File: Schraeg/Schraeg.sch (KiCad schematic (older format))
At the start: 56 parts, among them U1 TL074, U2 TL074, U3 V2164

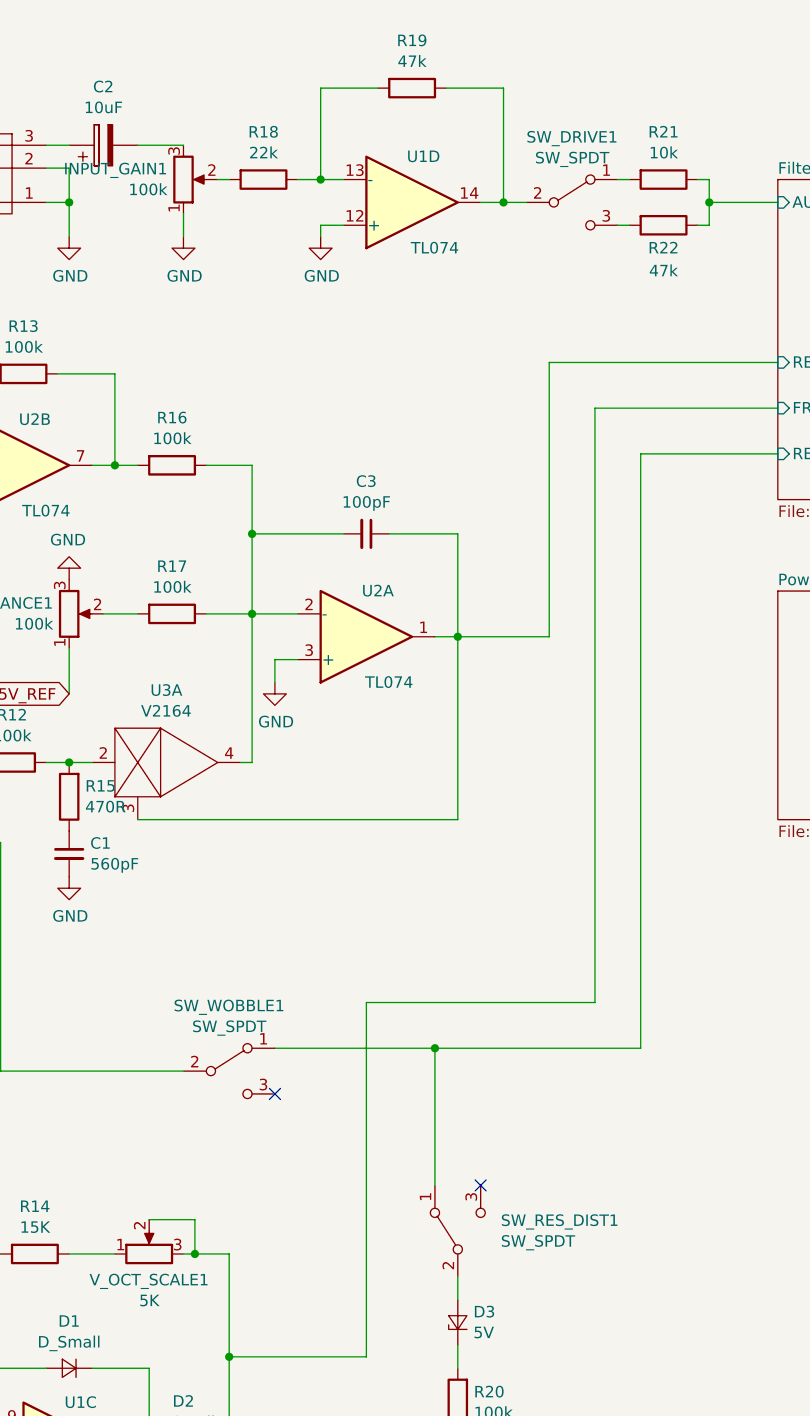
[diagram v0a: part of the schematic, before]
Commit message: Finished v0.2
* Flipped switches
* Enlarged switch holes
* Enlarged and enovaled pot support holes
* Reduced jack socket hole sizes
* Improved component and component reference locations

Archived v0.1 (previously know as the 2019 edition) and
re-exported schematics, gerbers, interactive BOM etc for
the 2021 Edition (v0.2).
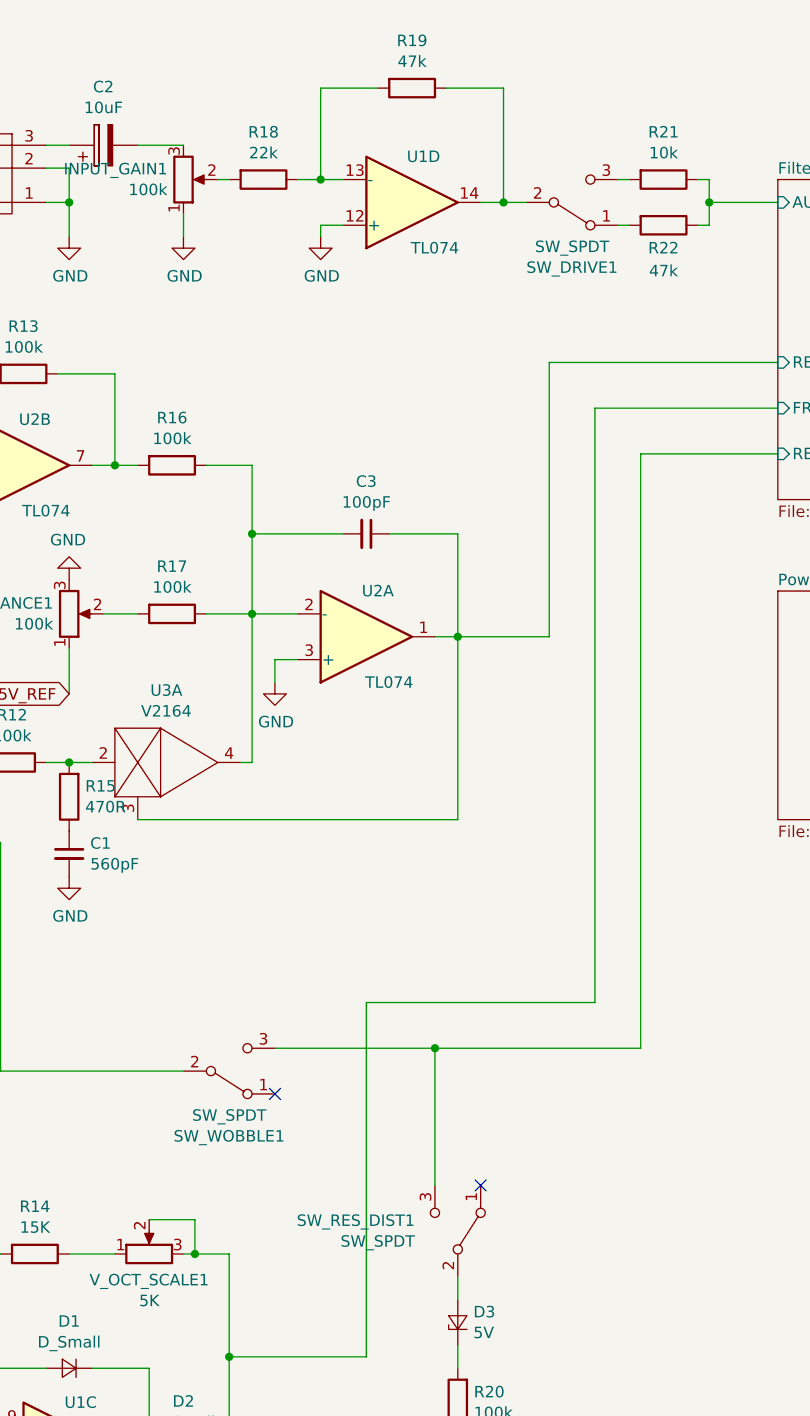
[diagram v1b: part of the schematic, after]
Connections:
- net Filter Core/RES_MOD: now also SW_RES_DIST1.3 (C), SW_WOBBLE1.3 (C); no longer SW_RES_DIST1.1 (A), SW_WOBBLE1.1 (A)
- net at SW_DRIVE1.1 (A): now also R22.2; no longer R21.2
- net at SW_DRIVE1.3 (C): now also R21.2; no longer R22.2
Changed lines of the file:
@@
 F 3 "" H 6500 1500 50  0001 C CNN
 	1    6500 1500
-	1    0    0    -1
+	1    0    0    1
 $EndComp
 $Comp
@@
 F 3 "" H 6000 6000 50  0001 C CNN
 	1    6000 6000
-	0    -1   -1   0
+	0    1    -1   0
 $EndComp
 $Comp
@@
 F 3 "" H 5000 5300 50  0001 C CNN
 	1    5000 5300
-	1    0    0    -1
-$EndComp
-Wire Wire Line
+	1    0    0    1
+$EndComp
+Wire Wire Line
